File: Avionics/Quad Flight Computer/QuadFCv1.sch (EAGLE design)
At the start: 86 parts, among them J1 10104111_MICROUSBAB, SW1 2-1437565-9, U1 74LVC4245APW, U10 ATMEGA32U2-MU, U2 TM4C123GH6PZ, U3 MPU-6050-1, U4 HMC5883LSMD, U8 SPI_PPM, X3 HWB, Y1 32.768KHZ, Y2 AWSCR-20.00CW-T, Y3 PRQC16.00SR5010X000

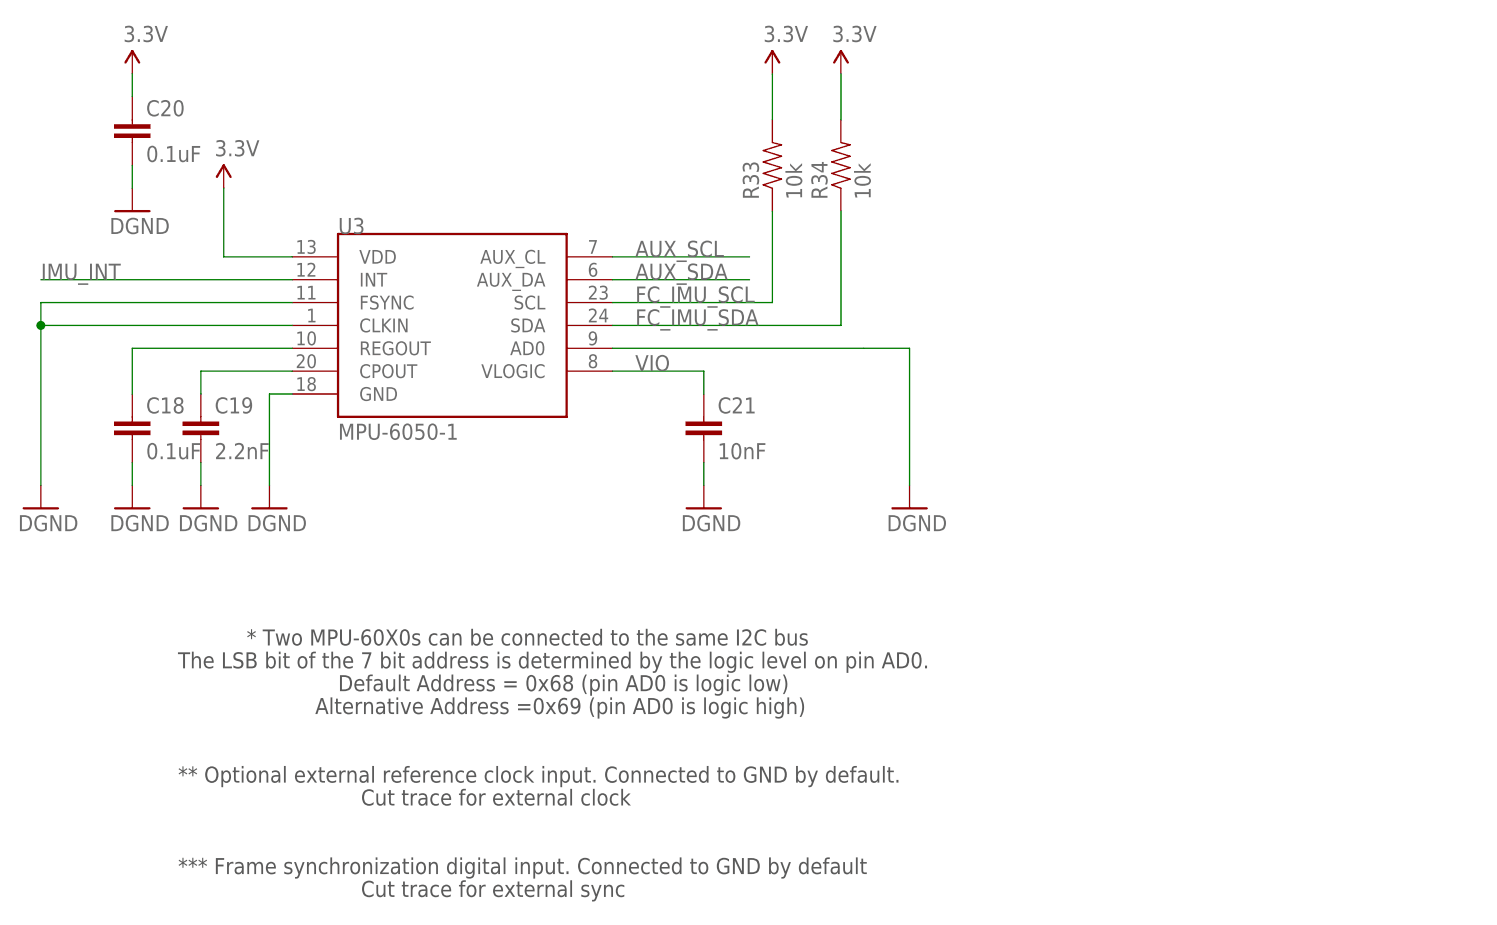
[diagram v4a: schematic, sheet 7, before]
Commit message: Exported all parts to libraries. Replaced IMU with MPU-6000.
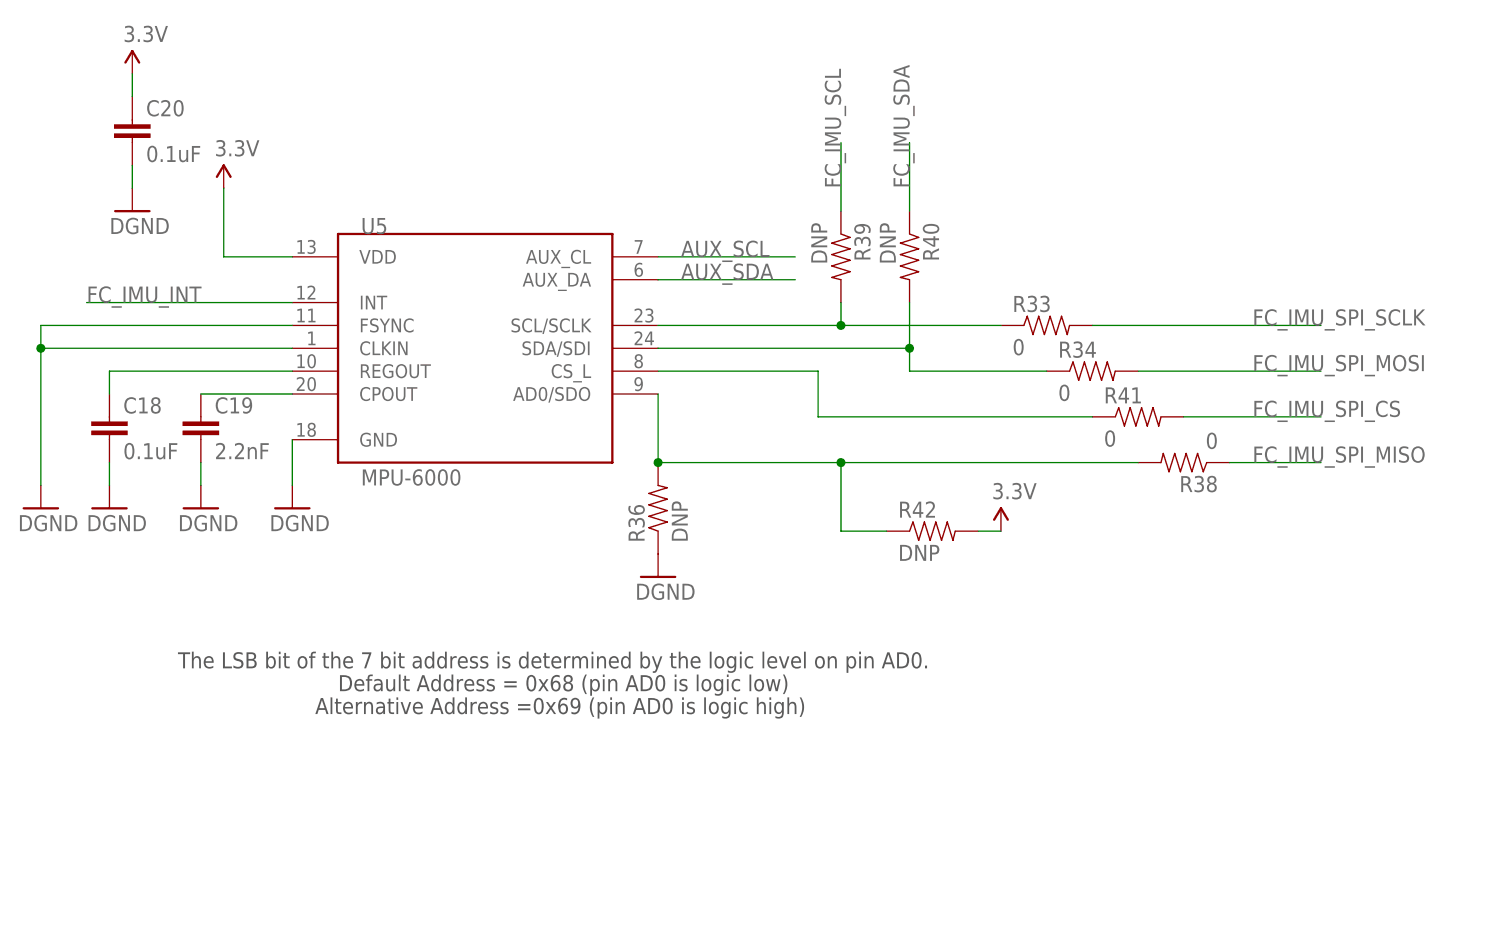
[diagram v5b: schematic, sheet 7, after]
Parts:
- removed C21: 10nF, SparkFun:CAP0402-CAP
- removed U3: MPU-6050-1, Testing:MPU-6050-1
- added R36, R39, R40, R42: DNP, SparkFun-Resistors:RESISTOR0603-RES
- added R38, R41: 0, SparkFun-Resistors:RESISTOR0603-RES
- added U5: MPU-6000, Invesense:MPU-6000
- C18, C19: device SparkFun:CAP0402-CAP -> SparkFun-Capacitors:CAP0603-CAP
- R33, R34: value 10k -> 0; device SparkFun:RESISTOR0402-RES -> SparkFun-Resistors:RESISTOR0603-RES
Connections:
- removed net IMU_INT: U3.INT
- removed net VIO: C21.1, U3.VLOGIC
- new net FC_IMU_INT: U5.INT
- new net FC_IMU_SPI_CS: R41.2
- new net FC_IMU_SPI_MISO: R38.1
- new net FC_IMU_SPI_MOSI: R34.2
- new net FC_IMU_SPI_SCLK: R33.2
- new net N$38: R33.1, R39.2, U5.SCL/SCLK
- new net N$39: R34.1, R40.2, U5.SDA/SDI
- new net N$40: R41.1, U5.CS_L
- new net N$41: R36.2, R38.2, R42.1, U5.AD0/SDO
- net 3.3V: now also R42.2, U5.VDD; no longer R33.2, R34.2, U3.VDD
- net AUX_SCL: now also U5.AUX_CL; no longer U3.AUX_CL
- net AUX_SDA: now also U5.AUX_DA; no longer U3.AUX_DA
- net FC_IMU_SCL: now also R39.1; no longer R33.1, U3.SCL
- net FC_IMU_SDA: now also R40.1; no longer R34.1, U3.SDA
- net GND: now also R36.1, U5.CLKIN, U5.FSYNC, U5.GND; no longer C21.2, U3.AD0, U3.CLKIN, U3.FSYNC, U3.GND
- net N$33: now also U5.CPOUT; no longer U3.CPOUT
- net N$34: now also U5.REGOUT; no longer U3.REGOUT
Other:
- note removed: "* Two MPU-60X0s can be connected to the same I2C bus"
- note removed: "** Optional external reference clock input. Connected to GND by default."
- note removed: "*** Frame synchronization digital input. Connected to GND by default"
- note removed: "Cut trace for external clock"
- note removed: "Cut trace for external sync"
- moved on the sheet: C18, R33, R34

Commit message: Connected sensor network and added pressure sensor
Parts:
- removed R36, R42: DNP, SparkFun-Resistors:RESISTOR0603-RES
- removed R38, R41: 0, SparkFun-Resistors:RESISTOR0603-RES
- added C21: 0.1uF, SparkFun-Capacitors:CAP0603-CAP
- added U6: MS5611-01BA, 3DRobotics:MS5611-01BA
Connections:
- net PPM_STATUS0 renamed FC_PPM_STATUS0
- net PPM_STATUS1 renamed FC_PPM_STATUS1
- removed net FC_IMU_SCL: R39.1, U2PORTG.PG0/I2C3SCL/M1FAULT1/PHA1/T4CCP0, U4.SCL
- removed net FC_IMU_SDA: R40.1, U2PORTG.PG1/I2C3SDA/M1FAULT2/PHB1/T4CCP1, U4.SDA
- removed net FC_IMU_SPI_CS: R41.2
- removed net FC_IMU_SPI_MISO: R38.1
- removed net FC_IMU_SPI_MOSI: R34.2
- removed net FC_IMU_SPI_SCLK: R33.2
- removed net FC_SSI3CLK: U2PORTK.PK0/M1FAULT0/SSI3CLK
- removed net FC_SSI3FSS: U2PORTK.PK1/M1FAULT1/SSI3FSS
- removed net FC_SSI3RX: U2PORTK.PK2/M1FAULT2/SSI3RX
- removed net FC_SSI3TX: U2PORTK.PK3/M1FAULT3/SSI3TX
- removed net N$38: R33.1, R39.2, U5.SCL/SCLK
- removed net N$39: R34.1, R40.2, U5.SDA/SDI
- removed net N$40: R41.1, U5.CS_L
- removed net N$41: R36.2, R38.2, R42.1, U5.AD0/SDO
- new net FC_IMU_CS_L: U2PORTK.PK1/M1FAULT1/SSI3FSS, U5.CS_L
- new net FC_IMU_MISO: U2PORTK.PK2/M1FAULT2/SSI3RX, U5.AD0/SDO
- new net FC_IMU_MOSI: U2PORTK.PK3/M1FAULT3/SSI3TX, U5.SDA/SDI
- new net FC_IMU_SCLK: U2PORTK.PK0/M1FAULT0/SSI3CLK, U5.SCL/SCLK
- new net FC_PPM_IN: R28.1
- new net FC_SENSE_SCL: R33.2, U2PORTG.PG0/I2C3SCL/M1FAULT1/PHA1/T4CCP0, U6.SCLK
- new net FC_SENSE_SDA: R34.2, U2PORTG.PG1/I2C3SDA/M1FAULT2/PHB1/T4CCP1, U6.SDI/SDA
- new net FC_USB_STATUS: R31.1
- new net MAG_SCL: R33.1, R39.1, U4.SCL
- new net MAG_SDA: R34.1, R40.1, U4.SDA
- net 3.3V: now also C21.1, U6.PS, U6.VDD; no longer R42.2
- net AUX_SCL: now also R39.2
- net AUX_SDA: now also R40.2
- net GND: now also C21.2, U6.CSB2, U6.GND; no longer R36.1

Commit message: Added 16MB flash chip for core event logging and mission profile configuration. Internal EEPROM will be used for core configuration (failsafe modes, dead zones, etc), external flash will store mission parameters and user settings.
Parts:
- removed R46, R47, R51: 1k, SparkFun:RESISTOR0402-RES
- added R36: 1k, SparkFun:RESISTOR0402-RES
- added R38: DNP, SparkFun-Resistors:RESISTOR0603-RES
- added R41: 0, SparkFun-Resistors:RESISTOR0603-RES
- added U7: MS5611-01BA, 3DRobotics:MS5611-01BA
- added U9: S25FL127S, Shared Libraries:S25FL127S
- C1: value 1uF -> 0.1uF; device SparkFun-Passives:CAP0603-CAP -> SparkFun-Capacitors:CAP0603-CAP
- C12: value 18pF -> 1uF
- C14: value .1uF -> 1uF; device SparkFun:CAP0402-CAP -> SparkFun-Passives:CAP0603-CAP
- C15: value 0.1uF -> .1uF; device SparkFun-Capacitors:CAP0603-CAP -> SparkFun:CAP0402-CAP
- C16: value .1uF -> 1uF
- C17: value 1uF -> .1uF
- C18: device SparkFun-Capacitors:CAP0603-CAP -> SparkFun:CAP0402-CAP
- C19: value 2.2nF -> 0.1uF
- C2, C3: value 1uF -> 0.1uF
- C20: value 0.1uF -> 2.2nF; device SparkFun:CAP0402-CAP -> SparkFun-Capacitors:CAP0603-CAP
- C21: value 0.1uF -> 4.7uF
- C23: value 4.7uF -> 0.1uF
- C7: value 0.1uF -> 18pF
- C9: value 0.1uF -> 1uF
- R13: value 0 -> 220; device SparkFun-Resistors:RESISTOR0805-RES -> SparkFun-Resistors:RESISTOR0603-RES
- R22: value 10K -> 220
- R23: value 49.9K -> 220
- R24: value 22 -> 220; device Shared Libraries:RESISTOR0603-RES -> SparkFun-Resistors:RESISTOR0603-RES
- R25: value 22-DNP -> 220; device Shared Libraries:RESISTOR0603-RES -> SparkFun-Resistors:RESISTOR0603-RES
- R26: value 22-DNP -> 49.9K; device Shared Libraries:RESISTOR0603-RES -> SparkFun-Resistors:RESISTOR0603-RES
- R27: value 0 -> 10K; device Shared Libraries:RESISTOR0603-RES -> SparkFun-Resistors:RESISTOR0603-RES
- R28: value 1K -> 1M
- R29: value 1M -> 10K
- R3: value 22 -> 22-DNP
- R31: value 1k -> 1K
- R33, R34: value 0 -> 1k; device SparkFun-Resistors:RESISTOR0603-RES -> SparkFun:RESISTOR0402-RES
- R37: value 10K -> 1k
- R4: value 0 -> 22; device SparkFun-Resistors:RESISTOR0805-RES -> Shared Libraries:RESISTOR0603-RES
- R40: value DNP -> 0
- R5: value 220 -> 22-DNP; device SparkFun-Resistors:RESISTOR0603-RES -> Shared Libraries:RESISTOR0603-RES
- R6: value 220 -> 0; device SparkFun-Resistors:RESISTOR0603-RES -> Shared Libraries:RESISTOR0603-RES
- R7: value 220 -> 22; device SparkFun-Resistors:RESISTOR0603-RES -> Shared Libraries:RESISTOR0603-RES
- R8, R9: value 220 -> 0; device SparkFun-Resistors:RESISTOR0603-RES -> SparkFun-Resistors:RESISTOR0805-RES
- U1: value 74LVC4245APW -> TM4C123GH6PZ; device Shared Libraries:74LVC4245APW -> Shared Libraries:TM4C123GH6PZ
- U2: value TM4C123GH6PZ -> 74LVC4245APW; device Shared Libraries:TM4C123GH6PZ -> Shared Libraries:74LVC4245APW
- U4: value HMC5883LSMD -> SPI_PPM; device Shared Libraries:HMC5883LSMD -> SparkFunv2:AVR_SPI_PRG_6NS
- U6: value MS5611-01BA -> HMC5883LSMD; device 3DRobotics:MS5611-01BA -> Shared Libraries:HMC5883LSMD
- U8: value SPI_PPM -> 74AUP1G19GW; device SparkFunv2:AVR_SPI_PRG_6NS -> Shared Libraries:74AUP1G19GW
- renumbered F2 to F1, LED4 to LED2, LED5 to LED1, LED7 to LED3, U10 to U3, X3 to X1
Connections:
- removed net FC_SSI0CLK: U2PORTA.PA2/SSI0CLK
- removed net FC_SSI0FSS: U2PORTA.PA3/SSI0FSS
- removed net FC_SSI0RX: U2PORTA.PA4/SSI0RX
- removed net FC_SSI0TX: U2PORTA.PA5/SSI0TX
- new net FC_MEM_CLK: U1PORTA.PA2/SSI0CLK, U9.SCK
- new net FC_MEM_FSS: U1PORTA.PA3/SSI0FSS, U8.EN_L
- new net FC_MEM_MISO: U1PORTA.PA4/SSI0RX, U9.SO
- new net FC_MEM_MOSI: U1PORTA.PA5/SSI0TX, U9.SI
- new net FC_MEM_SEL: U8.SEL
- new net FLASH_CS_L: U8.1Y, U9.CS_L
- new net SD_CS_L: U8.2Y
- net 3.3V: now also C1.1, C13.1, C18.1, C2.1, C23.1, R26.2, U1PWR.VBAT, U1PWR.VDD@1, U1PWR.VDD@2, U1PWR.VDD@3, U1PWR.VDD@4, U1PWR.VDD@5, U1PWR.VDD@6, U1PWR.VDD@7, U1PWR.VDD@8, U1PWR.VDDA, U2VCC3@1.1, U2VCC3@2.1, U6.S1, U6.VDDIO, U7.PS, U7.VDD, U8.VCC, U9.VCC; no longer C20.1, C21.1, C4.1, C7.1, C9.1, R23.2, U1VCC3@1.1, U1VCC3@2.1, U2PWR.VBAT, U2PWR.VDD@1, U2PWR.VDD@2, U2PWR.VDD@3, U2PWR.VDD@4, U2PWR.VDD@5, U2PWR.VDD@6, U2PWR.VDD@7, U2PWR.VDD@8, U2PWR.VDDA, U4.S1, U4.VDD, U4.VDDIO, U6.PS
- net 5V: now also C15.1, C17.1, R29.2, R33.1, R34.1, R8.2, R9.2, U2VCC5.1, U4.2; no longer C14.1, C16.1, R13.2, R32.1, R37.2, R4.2, R51.1, U1VCC5.1, U8.2
- net AUX_SCL: now also R38.2; no longer R39.2
- net AUX_SDA: now also R39.2; no longer R40.2
- net FC_AIN0: now also U1PORTE.PE3/AIN0; no longer U2PORTE.PE3/AIN0
- net FC_AIN1: now also U1PORTE.PE2/AIN1; no longer U2PORTE.PE2/AIN1
- net FC_AIN20: now also U1PORTE.PE7/AIN20/CAN1TX/U1RI; no longer U2PORTE.PE7/AIN20/CAN1TX/U1RI
- net FC_AIN21: now also U1PORTE.PE6/AIN21/CAN1RX; no longer U2PORTE.PE6/AIN21/CAN1RX
- net FC_AIN4: now also U1PORTD.PD7/AIN4/M0FAULT1/NMI/PHB0/U2TX/WT5CCP1; no longer U2PORTD.PD7/AIN4/M0FAULT1/NMI/PHB0/U2TX/WT5CCP1
- net FC_AIN5: now also U1PORTD.PD6/AIN5/M0FAULT0/PHA0/U2RX/WT5CCP0; no longer U2PORTD.PD6/AIN5/M0FAULT0/PHA0/U2RX/WT5CCP0
- net FC_IMU_CS_L: now also U1PORTK.PK1/M1FAULT1/SSI3FSS; no longer U2PORTK.PK1/M1FAULT1/SSI3FSS
- net FC_IMU_MISO: now also U1PORTK.PK2/M1FAULT2/SSI3RX; no longer U2PORTK.PK2/M1FAULT2/SSI3RX
- net FC_IMU_MOSI: now also U1PORTK.PK3/M1FAULT3/SSI3TX; no longer U2PORTK.PK3/M1FAULT3/SSI3TX
- net FC_IMU_SCLK: now also U1PORTK.PK0/M1FAULT0/SSI3CLK; no longer U2PORTK.PK0/M1FAULT0/SSI3CLK
- net FC_JTAG_TCK: now also U1PORTC.PC0/SWCLK/T4CCP0/TCK; no longer U2PORTC.PC0/SWCLK/T4CCP0/TCK
- net FC_JTAG_TDI: now also U1PORTC.PC2/T5CCP0/TDI; no longer U2PORTC.PC2/T5CCP0/TDI
- net FC_JTAG_TDO: now also U1PORTC.PC3/SWO/T5CCP1/TDO; no longer U2PORTC.PC3/SWO/T5CCP1/TDO
- net FC_JTAG_TMS: now also U1PORTC.PC1/SWDIO/T4CCP1/TMS; no longer U2PORTC.PC1/SWDIO/T4CCP1/TMS
- net FC_MAG_DRDY_L: now also U6.DRDY; no longer U4.DRDY
- net FC_PA6: now also U1PORTA.PA6/I2C1SCL/M1PWM2; no longer U2PORTA.PA6/I2C1SCL/M1PWM2
- net FC_PA7: now also U1PORTA.PA7/I2C1SDA/M1PWM3; no longer U2PORTA.PA7/I2C1SDA/M1PWM3
- net FC_PB2: now also U1PORTB.PB2/I2C0SCL/T3CCP0; no longer U2PORTB.PB2/I2C0SCL/T3CCP0
- net FC_PB3: now also U1PORTB.PB3/I2C0SDA/T3CCP1; no longer U2PORTB.PB3/I2C0SDA/T3CCP1
- net FC_PB4: now also U1PORTB.PB4/AIN10/CAN0RX/M0PWM2/SSI2CLK/T1CCP0; no longer U2PORTB.PB4/AIN10/CAN0RX/M0PWM2/SSI2CLK/T1CCP0
- net FC_PB5: now also U1PORTB.PB5/AIN11/CAN0TX/M0PWM3/SSI2FSS/T1CCP1; no longer U2PORTB.PB5/AIN11/CAN0TX/M0PWM3/SSI2FSS/T1CCP1
- net FC_PD0: now also U1PORTD.PD0/AIN15/I2C3SCL/M0PWM6/M1PWM0/SSI1CLK/SSI3CLK/WT2CCP0; no longer U2PORTD.PD0/AIN15/I2C3SCL/M0PWM6/M1PWM0/SSI1CLK/SSI3CLK/WT2CCP0
- net FC_PD1: now also U1PORTD.PD1/AIN14/I2C3SDA/M0PWM7/M1PWM1/SSI1FSS/SSI3FSS/WT2CCP1; no longer U2PORTD.PD1/AIN14/I2C3SDA/M0PWM7/M1PWM1/SSI1FSS/SSI3FSS/WT2CCP1
- net FC_PD2: now also U1PORTD.PD2/AIN13/M0FAULT0/SSI1RX/SSI3RX/USB0EPEN/WT3CCP0; no longer U2PORTD.PD2/AIN13/M0FAULT0/SSI1RX/SSI3RX/USB0EPEN/WT3CCP0
- net FC_PD3: now also U1PORTD.PD3/AIN12/IDX0/SSI1TX/SSI3TX/USB0PFLT/WT3CCP1; no longer U2PORTD.PD3/AIN12/IDX0/SSI1TX/SSI3TX/USB0PFLT/WT3CCP1
- net FC_PD4: now also U1PORTD.PD4/AIN7/U6RX/WT4CCP0; no longer U2PORTD.PD4/AIN7/U6RX/WT4CCP0
- net FC_PD5: now also U1PORTD.PD5/AIN6/U6TX/WT4CCP1; no longer U2PORTD.PD5/AIN6/U6TX/WT4CCP1
- net FC_PE4: now also U1PORTE.PE4/AIN9/CAN0RX/I2C2SCL/M0PWM4/M1PWM2/U5RX; no longer U2PORTE.PE4/AIN9/CAN0RX/I2C2SCL/M0PWM4/M1PWM2/U5RX
- net FC_PE5: now also U1PORTE.PE5/AIN8/CAN0TX/I2C2SDA/M0PWM5/M1PWM3/U5TX; no longer U2PORTE.PE5/AIN8/CAN0TX/I2C2SDA/M0PWM5/M1PWM3/U5TX
- net FC_PF0: now also U1PORTF.PF0/C0O/CAN0RX/M1PWM4/NMI/PHA0/SSI1RX/T0CCP0/TRD2/U1RTS; no longer U2PORTF.PF0/C0O/CAN0RX/M1PWM4/NMI/PHA0/SSI1RX/T0CCP0/TRD2/U1RTS
- net FC_PF1: now also U1PORTF.PF1/C1O/M1PWM5/PHB0/SSI1TX/T0CCP1/TRD1/U1CTS; no longer U2PORTF.PF1/C1O/M1PWM5/PHB0/SSI1TX/T0CCP1/TRD1/U1CTS
- net FC_PF2: now also U1PORTF.PF2/C2O/M0FAULT0/M1PWM6/SSI1CLK/T1CCP0/TRD0/U1DCD; no longer U2PORTF.PF2/C2O/M0FAULT0/M1PWM6/SSI1CLK/T1CCP0/TRD0/U1DCD
- net FC_PF3: now also U1PORTF.PF3/CAN0TX/M0FAULT1/M1PWM7/SSI1FSS/T1CCP1/TRCLK/U1DSR; no longer U2PORTF.PF3/CAN0TX/M0FAULT1/M1PWM7/SSI1FSS/T1CCP1/TRCLK/U1DSR
- net FC_PF4: now also U1PORTF.PF4/IDX0/M0FAULT2/M1FAULT0/T2CCP0/TRD3/U1DTR/USB0EPEN; no longer U2PORTF.PF4/IDX0/M0FAULT2/M1FAULT0/T2CCP0/TRD3/U1DTR/USB0EPEN
- net FC_PF5: now also U1PORTF.PF5/M0FAULT3/T2CCP1/USB0PFLT; no longer U2PORTF.PF5/M0FAULT3/T2CCP1/USB0PFLT
- net FC_PF6: now also U1PORTF.PF6/I2C2SCL/T3CCP0; no longer U2PORTF.PF6/I2C2SCL/T3CCP0
- net FC_PF7: now also U1PORTF.PF7/I2C2SDA/M1FAULT0/T3CCP1; no longer U2PORTF.PF7/I2C2SDA/M1FAULT0/T3CCP1
- net FC_PG2: now also U1PORTG.PG2/I2C4SCL/M0FAULT1/M1PWM0/T5CCP0; no longer U2PORTG.PG2/I2C4SCL/M0FAULT1/M1PWM0/T5CCP0
- net FC_PG3: now also U1PORTG.PG3/I2C4SDA/M0FAULT2/M1PWM1/PHA1/T5CCP1; no longer U2PORTG.PG3/I2C4SDA/M0FAULT2/M1PWM1/PHA1/T5CCP1
- net FC_PG4: now also U1PORTG.PG4/I2C1SCL/M0PWM4/M1PWM2/PHB1/U2RX/USB0EPEN/MT0CCP0; no longer U2PORTG.PG4/I2C1SCL/M0PWM4/M1PWM2/PHB1/U2RX/USB0EPEN/MT0CCP0
- net FC_PG5: now also U1PORTG.PG5/I2C1SDA/IDX1/M0PWM5/M1PWM3/U2TX/USB0PFLT/WT0CCP1; no longer U2PORTG.PG5/I2C1SDA/IDX1/M0PWM5/M1PWM3/U2TX/USB0PFLT/WT0CCP1
- net FC_PG6: now also U1PORTG.PG6/C2+/I2C5SCL/M0PWM6/WT1CCP0; no longer U2PORTG.PG6/C2+/I2C5SCL/M0PWM6/WT1CCP0
- net FC_PG7: now also U1PORTG.PG7/C2-/I2C5SDA/IDX1/M0PWM7/WT1CCP1; no longer U2PORTG.PG7/C2-/I2C5SDA/IDX1/M0PWM7/WT1CCP1
- net FC_PJ2: now also U1PORTJ.PJ2/IDX0/T2CCP0/U5RX; no longer U2PORTJ.PJ2/IDX0/T2CCP0/U5RX
- net FC_PPM_IN: now also R31.1; no longer R28.1
- net FC_PPM_STATUS0: now also R37.1; no longer R47.1
- net FC_PPM_STATUS1: now also R32.1; no longer R46.1
- net FC_PWMOUT1: now also U1PORTH.PH0/AIN16/M0FAULT0/M0PWM0/SSI3CLK/WT2CCP0, U2G$1.B1; no longer U1G$1.B1, U2PORTH.PH0/AIN16/M0FAULT0/M0PWM0/SSI3CLK/WT2CCP0
- net FC_PWMOUT2: now also U1PORTH.PH1/AIN17/IDX0/M0FAULT1/M0PWM1/SSI3FSS/WT2CCP1, U2G$1.B2; no longer U1G$1.B2, U2PORTH.PH1/AIN17/IDX0/M0FAULT1/M0PWM1/SSI3FSS/WT2CCP1
- net FC_PWMOUT3: now also U1PORTH.PH2/AIN18/M0FAULT2/M0PWM2/SSI3RX/WT5CCP0, U2G$1.B3; no longer U1G$1.B3, U2PORTH.PH2/AIN18/M0FAULT2/M0PWM2/SSI3RX/WT5CCP0
- net FC_PWMOUT4: now also U1PORTH.PH3/AIN19/M0FAULT3/M0PWM3/SSI3TX/WT5CCP1, U2G$1.B4; no longer U1G$1.B4, U2PORTH.PH3/AIN19/M0FAULT3/M0PWM3/SSI3TX/WT5CCP1
- net FC_PWMOUT5: now also U1PORTH.PH4/M0PWM4/PHA0/SSI2CLK/WT3CCP0, U2G$1.B5; no longer U1G$1.B5, U2PORTH.PH4/M0PWM4/PHA0/SSI2CLK/WT3CCP0
- net FC_PWMOUT6: now also U1PORTH.PH5/M0PWM5/PHB0/SSI2FSS/WT3CCP1, U2G$1.B6; no longer U1G$1.B6, U2PORTH.PH5/M0PWM5/PHB0/SSI2FSS/WT3CCP1
- net FC_PWMOUT7: now also U1PORTH.PH6/M0PWM6/SSI2RX/WT4CCP0, U2G$1.B7; no longer U1G$1.B7, U2PORTH.PH6/M0PWM6/SSI2RX/WT4CCP0
- net FC_PWMOUT8: now also U1PORTH.PH7/M0PWM7/SSI2TX/WT4CCP1, U2G$1.B8; no longer U1G$1.B8, U2PORTH.PH7/M0PWM7/SSI2TX/WT4CCP1
- net FC_PWMOUT_ARM_L: now also R26.1, U2G$1.OE_L; no longer R23.1, U1G$1.OE_L
- net FC_RESET_L: now also C4.1, U1SPECIAL.RST_L; no longer C15.1, U2SPECIAL.RST_L
- net FC_SENSE_SCL: now also R41.2, U1PORTG.PG0/I2C3SCL/M1FAULT1/PHA1/T4CCP0, U7.SCLK; no longer R33.2, U2PORTG.PG0/I2C3SCL/M1FAULT1/PHA1/T4CCP0, U6.SCLK
- net FC_SENSE_SDA: now also R40.2, U1PORTG.PG1/I2C3SDA/M1FAULT2/PHB1/T4CCP1, U7.SDI/SDA; no longer R34.2, U2PORTG.PG1/I2C3SDA/M1FAULT2/PHB1/T4CCP1, U6.SDI/SDA
- net FC_U0RX: now also U1PORTA.PA0/CAN1RX/U0RX; no longer U2PORTA.PA0/CAN1RX/U0RX
- net FC_U0TX: now also U1PORTA.PA1/CAN1TX/U0TX; no longer U2PORTA.PA1/CAN1TX/U0TX
- net FC_U1RX: now also U1PORTC.PC4/C1-/IDX1/M0PWM6/U1RTS/U1RX/U4RX/WT0CCP0; no longer U2PORTC.PC4/C1-/IDX1/M0PWM6/U1RTS/U1RX/U4RX/WT0CCP0
- net FC_U1TX: now also U1PORTC.PC5/C1+/M0PWM7/PHA1/U1CTS/U1TX/U4TX/WT0CCP1; no longer U2PORTC.PC5/C1+/M0PWM7/PHA1/U1CTS/U1TX/U4TX/WT0CCP1
- net FC_U3RX: now also U1PORTC.PC6/C0+/PHB1/U3RX/USB0EPEN/WT1CCP0; no longer U2PORTC.PC6/C0+/PHB1/U3RX/USB0EPEN/WT1CCP0
- net FC_U3TX: now also U1PORTC.PC7/C0-/U3TX/USB0PFLT/WT1CCP1; no longer U2PORTC.PC7/C0-/U3TX/USB0PFLT/WT1CCP1
- net FC_U7RX: now also U1PORTE.PE0/AIN3/U7RX; no longer U2PORTE.PE0/AIN3/U7RX
- net FC_U7TX: now also U1PORTE.PE1/AIN2/U7TX; no longer U2PORTE.PE1/AIN2/U7TX
- net FC_USB0DM: now also R7.1, U1PORTJ.PJ0/T1CCP0/U4RX/USB0DM; no longer R3.1, U2PORTJ.PJ0/T1CCP0/U4RX/USB0DM
- net FC_USB0DP: now also R4.1, U1PORTJ.PJ1/T1CCP1/U4TX/USB0DP; no longer R24.1, U2PORTJ.PJ1/T1CCP1/U4TX/USB0DP
- net FC_USB0ID: now also R6.1, U1PORTB.PB0/T2CCP0/U1RX/USB0ID; no longer R27.1, U2PORTB.PB0/T2CCP0/U1RX/USB0ID
- net FC_USB0VBUS: now also U1PORTB.PB1/T2CCP1/U1TX/USB0VBUS; no longer U2PORTB.PB1/T2CCP1/U1TX/USB0VBUS
- net FC_USB_STATUS: now also R36.1; no longer R31.1
- net GND: now also C1.2, C12.2, C14.1, R27.1, U1PWR.GND@1, U1PWR.GND@2, U1PWR.GND@3, U1PWR.GND@4, U1PWR.GND@5, U1PWR.GND@6, U1PWR.GND@7, U1PWR.GND@8, U1PWR.GNDA, U1PWR.VREFA-, U2GND@1.1, U2GND@2.1, U2GND@3.1, U4.6, U6.GND@1, U6.GND@2, U7.CSB2, U7.GND, U8.GND, U9.GND; no longer C1.1, C14.2, C7.2, R22.1, U1GND@1.1, U1GND@2.1, U1GND@3.1, U2PWR.GND@1, U2PWR.GND@2, U2PWR.GND@3, U2PWR.GND@4, U2PWR.GND@5, U2PWR.GND@6, U2PWR.GND@7, U2PWR.GND@8, U2PWR.GNDA, U2PWR.VREFA-, U4.GND@1, U4.GND@2, U6.CSB2, U6.GND, U8.6
- net GNDX: now also C7.2, U1PWR.GNDX; no longer C12.2, U2PWR.GNDX
- net MAG_SCL: now also R38.1, R41.1, U6.SCL; no longer R33.1, R39.1, U4.SCL
- net MAG_SDA: now also R39.1, U6.SDA; no longer R34.1, U4.SDA
- net N$1: now also JP2.3, R18.2; no longer JP1.3, R5.2
- net N$10: now also JP1.4, R11.2; no longer JP2.4, R15.2
- net N$11: now also JP1.5, R12.2; no longer JP2.5, R16.2
- net N$12: now also JP1.6, R13.2; no longer JP2.6, R17.2
- net N$13: now also JP1.7, R14.2; no longer JP2.7, R18.2
- net N$14: now also JP1.8, R15.2; no longer JP2.8, R19.2
- net N$15: now also JP1.9, R16.2; no longer JP2.9, R20.2
- net N$16: now also JP1.10, R17.2; no longer JP2.10, R21.2
- net N$17: now also C14.2, U1PWR.VREFA+; no longer C1.2, U2PWR.VREFA+
- net N$18: now also C12.1, C9.1, U1PWR.VDDC@1, U1PWR.VDDC@2; no longer C13.1, C2.1, U2PWR.VDDC@1, U2PWR.VDDC@2
- net N$19: now also C11.1, U1SPECIAL.XOSC1; no longer C12.1, U2SPECIAL.XOSC1
- net N$2: now also JP2.4, R19.2; no longer JP1.4, R6.2
- net N$20: now also R27.2, U2G$1.DIR; no longer R22.2, U1G$1.DIR
- net N$21: now also C7.1, U1SPECIAL.XOSC0; no longer C11.1, U2SPECIAL.XOSC0
- net N$22: now also U1SPECIAL.WAKE_L; no longer U2SPECIAL.WAKE_L
- net N$23: now also JP2.2, R9.1; no longer JP1.2, R4.1
- net N$24: now also U1SPECIAL.OSC0; no longer U2SPECIAL.OSC0
- net N$25: now also U1SPECIAL.OSC1; no longer U2SPECIAL.OSC1
- net N$26: now also JP1.2, R8.1; no longer JP2.2, R13.1
- net N$27: now also R6.2; no longer R27.2
- net N$28: now also R7.2; no longer R26.2
- net N$29: now also R4.2, R5.2; no longer R24.2, R25.2
- net N$3: now also JP2.5, R20.2; no longer JP1.5, R7.2
- net N$30: now also R33.2; no longer R35.2
- net N$31: now also R34.2; no longer R32.2
- net N$32: now also R35.2; no longer R51.2
- net N$33: now also C20.1; no longer C19.1
- net N$34: now also C19.1; no longer C18.1
- net N$35: now also C21.1, U6.C1; no longer C23.1, U4.C1
- net N$36: now also U6.SETP; no longer U4.SETP
- net N$37: now also U6.SETC; no longer U4.SETC
- net N$4: now also JP2.6, R21.2; no longer JP1.6, R8.2
- net N$5: now also JP2.7, R22.2; no longer JP1.7, R9.2
- net N$6: now also JP2.8, R23.2; no longer JP1.8, R10.2
- net N$7: now also JP2.9, R24.2; no longer JP1.9, R11.2
- net N$8: now also JP2.10, R25.2; no longer JP1.10, R12.2
- net N$9: now also JP1.3, R10.2; no longer JP2.3, R14.2
- net PPM_OUT: now also R31.2; no longer R28.2
- net PPM_PD0: now also R37.2; no longer R47.2
- net PPM_PD1: now also R32.2; no longer R46.2
- net PPM_RST: now also R29.1, U4.5; no longer R37.1, U8.5
- net PPM_USBDM: now also R3.1; no longer R26.1
- net PPM_USBDP: now also R5.1; no longer R25.1
- net PPM_USB_STATUS: now also R36.2; no longer R31.2
- net PWMIN1: now also R18.1; no longer R5.1
- net PWMIN2: now also R19.1, U4.3; no longer R6.1, U8.3
- net PWMIN3: now also R20.1, U4.4; no longer R7.1, U8.4
- net PWMIN4: now also R21.1, U4.1; no longer R8.1, U8.1
- net PWMIN5: now also R22.1; no longer R9.1
- net PWMIN6: now also R23.1; no longer R10.1
- net PWMIN7: now also R24.1; no longer R11.1
- net PWMIN8: now also R25.1; no longer R12.1
- net PWMOUT1: now also R10.1, U2G$1.A1; no longer R14.1, U1G$1.A1
- net PWMOUT2: now also R11.1, U2G$1.A2; no longer R15.1, U1G$1.A2
- net PWMOUT3: now also R12.1, U2G$1.A3; no longer R16.1, U1G$1.A3
- net PWMOUT4: now also R13.1, U2G$1.A4; no longer R17.1, U1G$1.A4
- net PWMOUT5: now also R14.1, U2G$1.A5; no longer R18.1, U1G$1.A5
- net PWMOUT6: now also R15.1, U2G$1.A6; no longer R19.1, U1G$1.A6
- net PWMOUT7: now also R16.1, U2G$1.A7; no longer R20.1, U1G$1.A7
- net PWMOUT8: now also R17.1, U2G$1.A8; no longer R21.1, U1G$1.A8
- net VUCAP: now also C16.1; no longer C17.1
- net XT1: now also R28.2; no longer R29.2
- net XT2: now also R28.1; no longer R29.1
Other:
- note added: "Internal Pullups"
